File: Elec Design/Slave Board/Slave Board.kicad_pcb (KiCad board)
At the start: 2 copper layers, 81.3 x 358.6 mm, 87 parts, among them J1 JTAG, J2 OSTTC020162, J3 OSTTC030162, J4 OSTTC020162, J5 OSTTC030162, J6 0022232041, M1 VID28-05, M2 VID28-05, M3 VID28-05, M4 VID28-05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

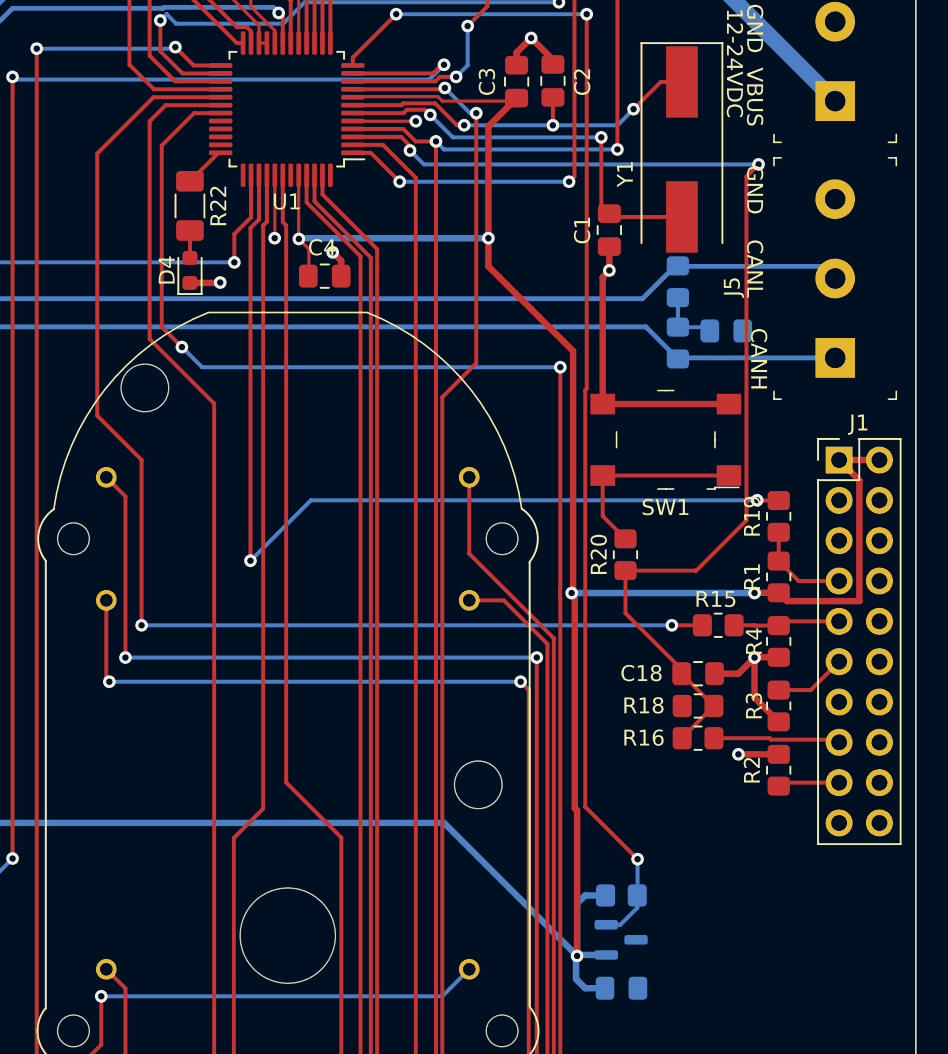
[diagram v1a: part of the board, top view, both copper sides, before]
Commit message: repositioned jtag header
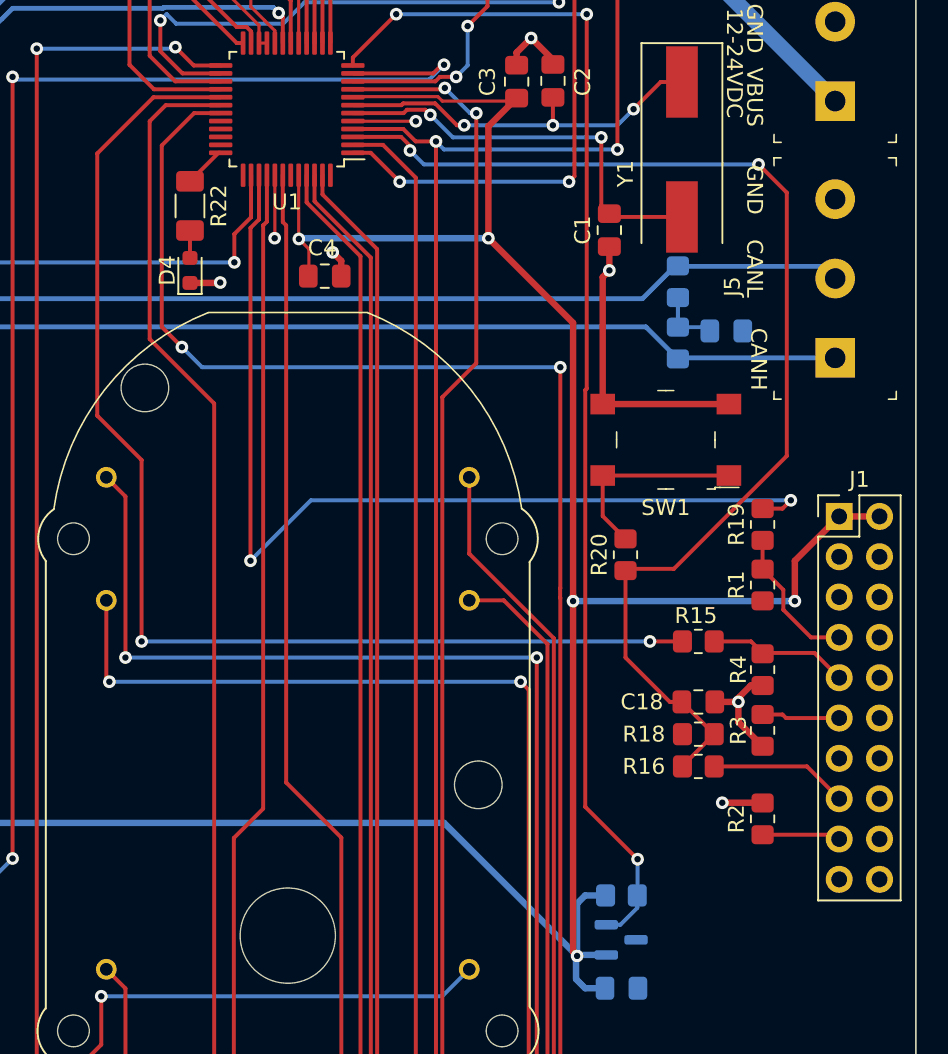
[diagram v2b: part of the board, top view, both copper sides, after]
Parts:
- moved J1 3.55 mm to (279.7, 230.9)
- moved R2 3.23 mm to (274.8, 249.9)
- moved R4 2.05 mm to (274.8, 240.5)
- moved R3 1.84 mm to (274.8, 244.4)
- moved C18 1.78 mm to (270.8, 242.6)
- moved R16 1.78 mm to (270.8, 246.6)
- moved R18 1.78 mm to (270.8, 244.6)
- moved R15 1.61 mm to (270.8, 238.8)
- moved R1 1.14 mm to (274.8, 235.2)
- moved R19 1.14 mm to (274.8, 231.4)
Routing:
- net +3.3V: track 798.5 -> 791.6 mm
- net Net-(J1-Pad7): track 6.14 -> 9.15 mm
- net Net-(C18-Pad2): track 71.8 -> 74.6 mm
- net /SWDIO: track 59.4 -> 62.1 mm
- net GND: track 102.3 -> 100.0 mm
- net Net-(J1-Pad9): track 6.73 -> 8.82 mm
- net Net-(J1-Pad17): track 3.89 -> 5.45 mm
- net /RESET: track 7.99 -> 8.95 mm
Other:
- board text added: "60R x2 + 1nF Bus Terminator"
- board text removed: "120R Bus Terminator"

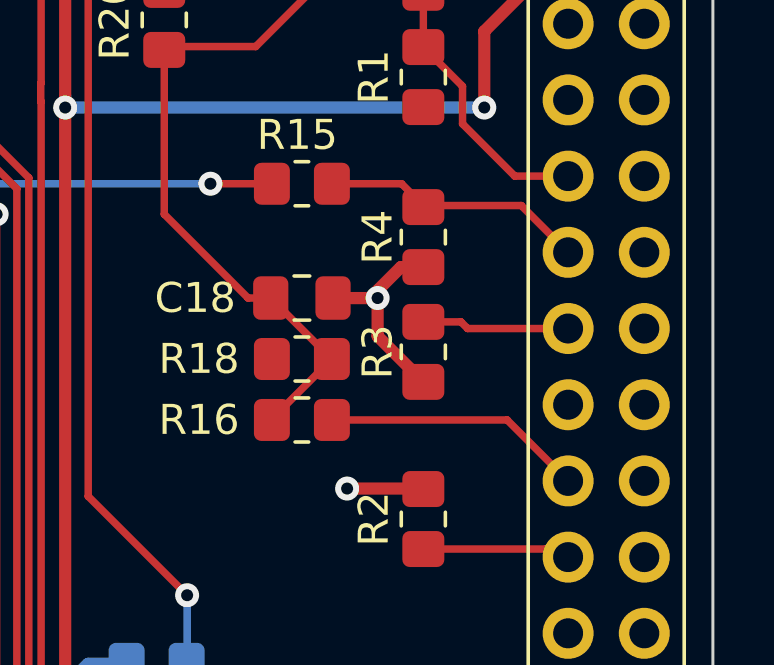
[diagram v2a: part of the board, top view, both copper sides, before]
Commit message: repositioned jtag header
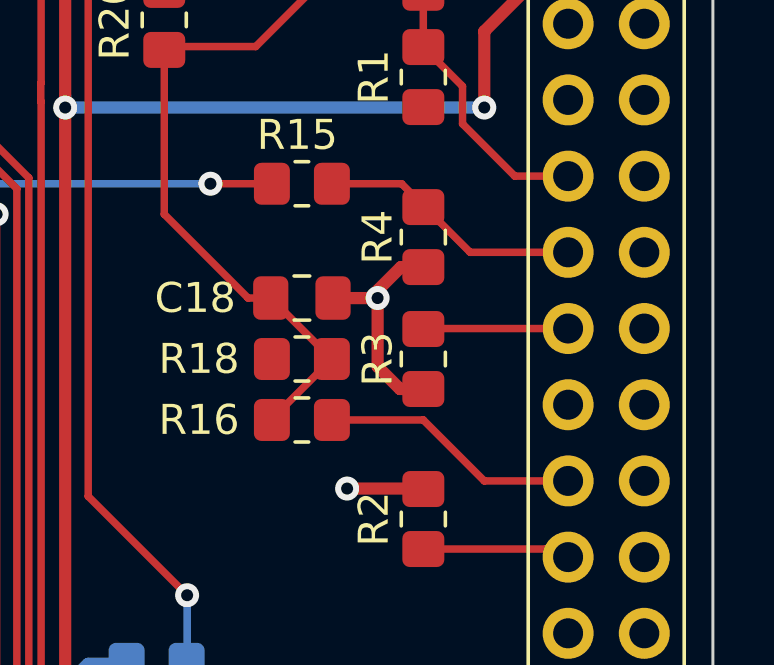
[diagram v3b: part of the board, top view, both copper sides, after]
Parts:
- moved R3 0.24 mm to (274.8, 244.6)
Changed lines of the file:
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@@
   )
   (footprint "Resistor_SMD:R_0805_2012Metric_Pad1.20x1.40mm_HandSolder" (layer "F.Cu")
-    (at 274.828 244.364 -90)
+    (at 274.828 244.602 -90)
     (descr "Resistor SMD 0805 (2012 Metric), square (rectangular) end terminal, IPC_7351 nominal with elongated pad for handsoldering. (Body size source: IPC-SM-782 page 72, https://www.pcb-3d.com/wordpress/wp-content/uploads/ipc-sm-782a_amendment_1_and_2.pdf), generated with kicad-footprint-generator")
     (tags "resistor handsolder")
@@
   )
   (segment (start 239.8776 196.6722) (end 239.8776 196.723) (width 0.2) (layer "F.Cu") (net 1))
+  (segment (start 273.304 244.856) (end 274.05 245.602) (width 0.4064) (layer "F.Cu") (net 1))
   (segment (start 211.328 192.158657) (end 211.898857 191.5878) (width 0.4064) (layer "F.Cu") (net 1))
   (segment (start 206.883 183.9975) (end 206.883 182.372) (width 0.4064) (layer "F.Cu") (net 1))
-  (segment (start 273.304 242.57) (end 273.304 243.84) (width 0.4064) (layer "F.Cu") (net 1))
   (segment (start 265.176 213.8895) (end 265.176 215.392) (width 0.4064) (layer "F.Cu") (net 1))
   (segment (start 236.22 98.2765) (end 236.22 97.282) (width 0.4064) (layer "F.Cu") (net 1))
@@
   (segment (start 259.334 201.666) (end 260.25 200.75) (width 0.4064) (layer "F.Cu") (net 1))
   (segment (start 261.62 202.12) (end 260.25 200.75) (width 0.4064) (layer "F.Cu") (net 1))
+  (segment (start 274.05 245.602) (end 274.59 245.602) (width 0.4064) (layer "F.Cu") (net 1))
   (segment (start 234.188 98.2765) (end 234.188 97.282) (width 0.4064) (layer "F.Cu") (net 1))
   (segment (start 215.4305 189.484) (end 215.9 189.9535) (width 0.4064) (layer "F.Cu") (net 1))
@@
   (segment (start 239.649 308.483) (end 237.236 310.896) (width 0.4064) (layer "F.Cu") (net 1))
   (segment (start 249.0305 205.994) (end 252.984 205.994) (width 0.2) (layer "F.Cu") (net 1))
+  (segment (start 273.304 242.57) (end 273.304 244.856) (width 0.4064) (layer "F.Cu") (net 1))
   (segment (start 271.8175 242.57) (end 273.05 242.57) (width 0.4064) (layer "F.Cu") (net 1))
   (segment (start 240.31 308.483) (end 239.649 308.483) (width 0.4064) (layer "F.Cu") (net 1))
@@
   (segment (start 209.7707 191.5878) (end 210.757143 191.5878) (width 0.4064) (layer "F.Cu") (net 1))
   (segment (start 234.188 97.282) (end 235.204 96.266) (width 0.4064) (layer "F.Cu") (net 1))
-  (segment (start 273.304 243.84) (end 274.828 245.364) (width 0.4064) (layer "F.Cu") (net 1))
   (segment (start 236.474 289.052) (end 237.49 288.036) (width 0.4064) (layer "F.Cu") (net 1))
   (segment (start 211.328 192.158657) (end 211.328 192.6535) (width 0.4064) (layer "F.Cu") (net 1))
@@
   (segment (start 212.3955 181.2545) (end 213.614 181.2545) (width 0.25) (layer "F.Cu") (net 9))
   (segment (start 238.76 212.878) (end 238.76 214.6045) (width 0.25) (layer "F.Cu") (net 10))
-  (segment (start 279.654 248.666) (end 277.622 246.634) (width 0.25) (layer "F.Cu") (net 11))
-  (segment (start 277.622 246.634) (end 271.78 246.634) (width 0.25) (layer "F.Cu") (net 11))
+  (segment (start 279.654 248.666) (end 276.86 248.666) (width 0.25) (layer "F.Cu") (net 11))
+  (segment (start 274.828 246.634) (end 271.78 246.634) (width 0.25) (layer "F.Cu") (net 11))
+  (segment (start 276.86 248.666) (end 274.828 246.634) (width 0.25) (layer "F.Cu") (net 11))
   (segment (start 279.654 248.666) (end 279.486 248.498) (width 0.25) (layer "F.Cu") (net 11))
   (segment (start 227.745097 103.793097) (end 232.156 108.204) (width 0.3048) (layer "F.Cu") (net 12))
@@
   (via (at 235.712 238.76) (size 0.8) (drill 0.4) (layers "F.Cu" "B.Cu") (net 51))
   (segment (start 267.732 238.76) (end 235.712 238.76) (width 0.25) (layer "B.Cu") (net 51))
-  (segment (start 276.082 243.364) (end 274.828 243.364) (width 0.25) (layer "F.Cu") (net 52))
-  (segment (start 276.304 243.586) (end 279.654 243.586) (width 0.25) (layer "F.Cu") (net 52))
-  (segment (start 276.082 243.364) (end 276.304 243.586) (width 0.25) (layer "F.Cu") (net 52))
+  (segment (start 279.654 243.586) (end 275.05 243.586) (width 0.25) (layer "F.Cu") (net 52))
+  (segment (start 275.05 243.586) (end 274.828 243.364) (width 0.25) (layer "F.Cu") (net 52))
   (segment (start 240.31 303.403) (end 238.125 303.403) (width 0.25) (layer "F.Cu") (net 54))
   (segment (start 228.092 313.436) (end 228.092 335.026) (width 0.25) (layer "F.Cu") (net 54))
@@
   (segment (start 276.135 236.765) (end 277.876 238.506) (width 0.25) (layer "F.Cu") (net 92))
   (segment (start 277.876 238.506) (end 279.654 238.506) (width 0.25) (layer "F.Cu") (net 92))
-  (segment (start 278.0938 239.4858) (end 274.828 239.4858) (width 0.25) (layer "F.Cu") (net 93))
-  (segment (start 279.654 241.046) (end 278.0938 239.4858) (width 0.25) (layer "F.Cu") (net 93))
+  (segment (start 279.654 241.046) (end 276.3882 241.046) (width 0.25) (layer "F.Cu") (net 93))
   (segment (start 274.1022 238.76) (end 271.78 238.76) (width 0.25) (layer "F.Cu") (net 93))
-  (segment (start 274.828 239.4858) (end 274.1022 238.76) (width 0.25) (layer "F.Cu") (net 93))
+  (segment (start 276.3882 241.046) (end 274.1022 238.76) (width 0.25) (layer "F.Cu") (net 93))
   (zone (net 5) (net_name "+5V") (layer "F.Cu") (hatch edge 0.508)
     (connect_pads (clearance 0.508))

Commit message: slave board cleanup
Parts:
- moved R18 2.05 mm to (268.7, 244.6)
- moved U13 1.02 mm to (210.6, 184.2), turned to 0 degrees
- moved R21 0.73 mm to (208.3, 188.2)
- moved D2 0.64 mm to (206.2, 184.8)
- moved R14 0.63 mm to (210.3, 180.1)
- moved C15 0.38 mm to (208.3, 191.9)
- moved D1 0.13 mm to (209.8, 195.7)
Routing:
- net Net-(J1-Pad7): track 9.15 -> 11.4 mm
- net +3.3V: track 791.6 -> 793.5 mm
- net Net-(C18-Pad2): track 74.6 -> 73.0 mm
- net /HAll A Hour - 1: track 192.3 -> 193.6 mm
- net Net-(D2-Pad2): track 1.97 -> 2.84 mm
- net GND: track 100.5 -> 99.8 mm
- net /HAll B Hour - 1: track 81.1 -> 81.7 mm

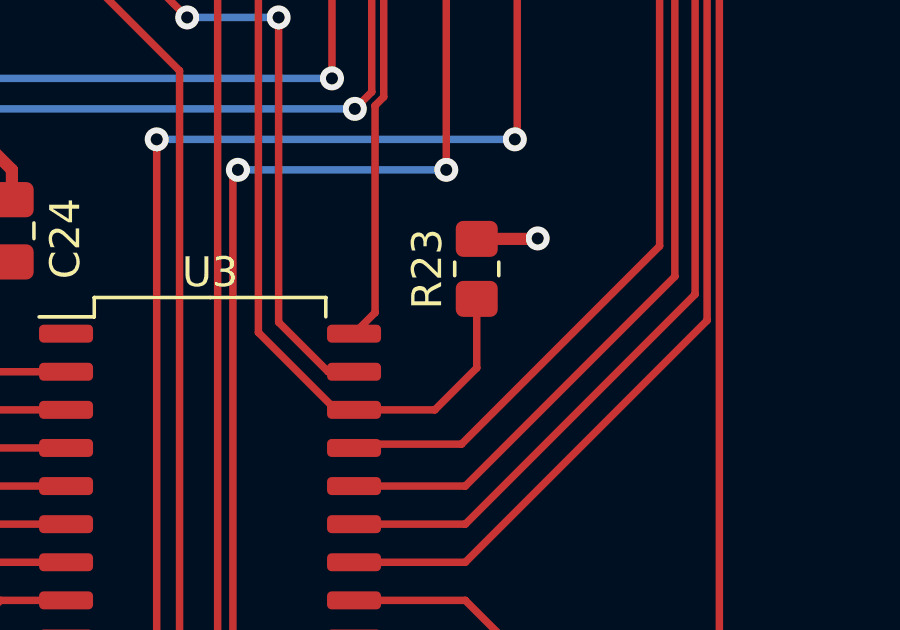
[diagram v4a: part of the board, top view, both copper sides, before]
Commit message: removed driver reset pulldown resistor
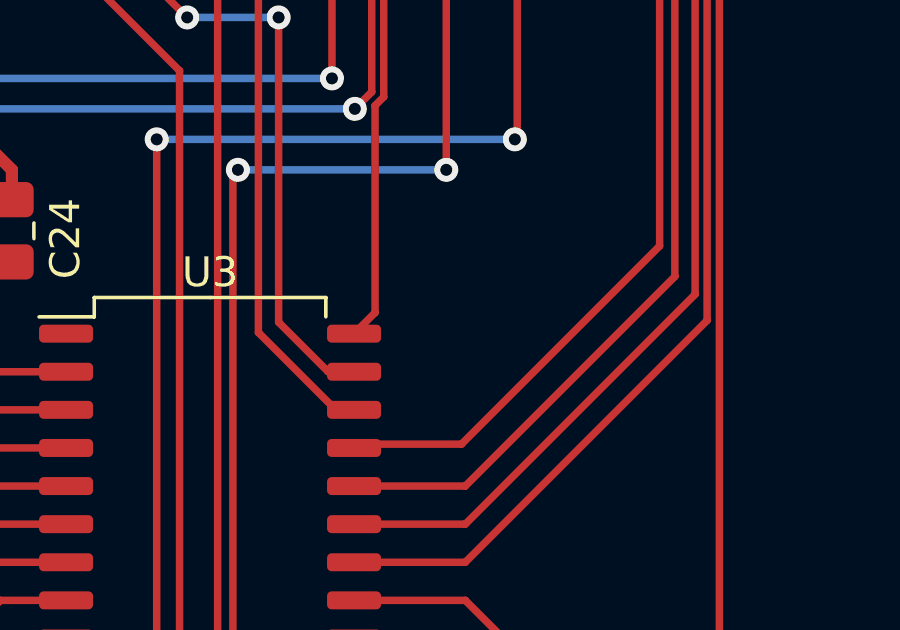
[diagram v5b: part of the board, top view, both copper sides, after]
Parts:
- removed R23: 10k, Resistor_SMD:R_0805_2012Metric_Pad1.20x1.40mm_HandSolder
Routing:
- net /Driver Reset: track 250.9 -> 243.9 mm
- net GND: track 99.8 -> 97.7 mm, vias 17 -> 16
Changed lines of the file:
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@@
     )
   )
-  (footprint "Resistor_SMD:R_0805_2012Metric_Pad1.20x1.40mm_HandSolder" (layer "F.Cu")
-    (at 254 292.354 90)
-    (descr "Resistor SMD 0805 (2012 Metric), square (rectangular) end terminal, IPC_7351 nominal with elongated pad for handsoldering. (Body size source: IPC-SM-782 page 72, https://www.pcb-3d.com/wordpress/wp-content/uploads/ipc-sm-782a_amendment_1_and_2.pdf), generated with kicad-footprint-generator")
-    (tags "resistor handsolder")
-    (property "DK_Datasheet_Link" "https://www.digikey.ca/en/htmldatasheets/production/781422/0/0/1/rmcf0805ft20m0.html?site=CA&lang=en&cur=CAD")
-    (property "DK_Detail_Page" "https://www.digikey.ca/en/products/detail/stackpole-electronics-inc/RMCF0805FT10K0/1760676")
-    (property "Sheetfile" "Slave Board.kicad_sch")
-    (property "Sheetname" "")
-    (attr smd)
-    (fp_text reference "R23" (at 0 -1.65 90) (layer "F.SilkS")
-        (effects (font (size 1 1) (thickness 0.15)))
-    )
-    (fp_text value "10k" (at 0 1.65 90) (layer "F.Fab")
-        (effects (font (size 1 1) (thickness 0.15)))
-    )
-    (fp_text user "${REFERENCE}" (at 0 0 90) (layer "F.Fab")
-        (effects (font (size 0.5 0.5) (thickness 0.08)))
-    )
-    (fp_line (start -0.227064 -0.735) (end 0.227064 -0.735)
-      (stroke (width 0.12) (type solid)) (layer "F.SilkS"))
-    (fp_line (start -0.227064 0.735) (end 0.227064 0.735)
-      (stroke (width 0.12) (type solid)) (layer "F.SilkS"))
-    (fp_line (start -1.85 -0.95) (end 1.85 -0.95)
-      (stroke (width 0.05) (type solid)) (layer "F.CrtYd"))
-    (fp_line (start -1.85 0.95) (end -1.85 -0.95)
-      (stroke (width 0.05) (type solid)) (layer "F.CrtYd"))
-    (fp_line (start 1.85 -0.95) (end 1.85 0.95)
-      (stroke (width 0.05) (type solid)) (layer "F.CrtYd"))
-    (fp_line (start 1.85 0.95) (end -1.85 0.95)
-      (stroke (width 0.05) (type solid)) (layer "F.CrtYd"))
-    (fp_line (start -1 -0.625) (end 1 -0.625)
-      (stroke (width 0.1) (type solid)) (layer "F.Fab"))
-    (fp_line (start -1 0.625) (end -1 -0.625)
-      (stroke (width 0.1) (type solid)) (layer "F.Fab"))
-    (fp_line (start 1 -0.625) (end 1 0.625)
-      (stroke (width 0.1) (type solid)) (layer "F.Fab"))
-    (fp_line (start 1 0.625) (end -1 0.625)
-      (stroke (width 0.1) (type solid)) (layer "F.Fab"))
-    (pad "1" smd roundrect (at -1 0 90) (size 1.2 1.4) (layers "F.Cu" "F.Paste" "F.Mask") (roundrect_rratio 0.2083333333)
-      (net 66 "/Driver Reset") (pintype "passive"))
-    (pad "2" smd roundrect (at 1 0 90) (size 1.2 1.4) (layers "F.Cu" "F.Paste" "F.Mask") (roundrect_rratio 0.2083333333)
-      (net 1 "GND") (pintype "passive"))
-    (model "${KICAD6_3DMODEL_DIR}/Resistor_SMD.3dshapes/R_0805_2012Metric.wrl"
-      (offset (xyz 0 0 0))
-      (scale (xyz 1 1 1))
-      (rotate (xyz 0 0 0))
-    )
-  )
   (footprint "LED_SMD:LED_0603_1608Metric" (layer "F.Cu")
     (at 206.248 184.785 -90)
@@
   (segment (start 238.76 216.1795) (end 240.6395 216.1795) (width 0.4064) (layer "F.Cu") (net 1))
   (segment (start 213.868 190.233343) (end 213.868 189.484) (width 0.4064) (layer "F.Cu") (net 1))
-  (segment (start 254 291.354) (end 256.016 291.354) (width 0.4064) (layer "F.Cu") (net 1))
   (segment (start 248.2875 214.7875) (end 247.75 214.25) (width 0.4064) (layer "F.Cu") (net 1))
   (segment (start 243.106 201.0695) (end 243.106 199.9514) (width 0.2) (layer "F.Cu") (net 1))
@@
   (segment (start 249.0185 205.982) (end 249.0305 205.994) (width 0.2) (layer "F.Cu") (net 1))
   (segment (start 240.6395 216.1795) (end 240.665 216.154) (width 0.4064) (layer "F.Cu") (net 1))
-  (segment (start 256.016 291.354) (end 256.032 291.338) (width 0.4064) (layer "F.Cu") (net 1))
   (segment (start 272.707 223.81) (end 264.757 223.81) (width 0.4064) (layer "F.Cu") (net 1))
   (segment (start 239.649 308.483) (end 237.236 310.896) (width 0.4064) (layer "F.Cu") (net 1))
@@
   (via (at 260.25 200.75) (size 0.8) (drill 0.4) (layers "F.Cu" "B.Cu") (net 1))
   (via (at 265.176 215.392) (size 0.8) (drill 0.4) (layers "F.Cu" "B.Cu") (net 1))
-  (via (at 256.032 291.338) (size 0.8) (drill 0.4) (layers "F.Cu" "B.Cu") (net 1))
   (via (at 216.027 178.943) (size 0.8) (drill 0.4) (layers "F.Cu" "B.Cu") (net 1))
   (segment (start 269.748 212.022) (end 265.3835 212.022) (width 0.25) (layer "F.Cu") (net 2))
@@
   (segment (start 246.0385 289.052) (end 252.984 289.052) (width 0.25) (layer "B.Cu") (net 65))
   (segment (start 268.8985 191.8575) (end 265.684 195.072) (width 0.25) (layer "F.Cu") (net 66))
-  (segment (start 252.603 297.053) (end 254 295.656) (width 0.25) (layer "F.Cu") (net 66))
   (segment (start 249.91 297.053) (end 249.301 297.053) (width 0.25) (layer "F.Cu") (net 66))
   (segment (start 254.254 282.5355) (end 254.6745 282.956) (width 0.25) (layer "F.Cu") (net 66))
@@
   (segment (start 268.8985 102.87) (end 268.8985 191.8575) (width 0.25) (layer "F.Cu") (net 66))
   (segment (start 254.254 207.264) (end 254.254 282.5355) (width 0.25) (layer "F.Cu") (net 66))
-  (segment (start 249.91 297.053) (end 252.603 297.053) (width 0.25) (layer "F.Cu") (net 66))
-  (segment (start 254 295.656) (end 254 293.354) (width 0.25) (layer "F.Cu") (net 66))
   (segment (start 246.7215 294.4735) (end 246.7215 283.1225) (width 0.25) (layer "F.Cu") (net 66))
   (segment (start 249.0185 206.482) (end 252.193402 206.482) (width 0.25) (layer "F.Cu") (net 66))
